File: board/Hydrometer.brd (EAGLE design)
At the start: 49.2 x 49.5 mm, 13 parts, among them IC2 REG1117

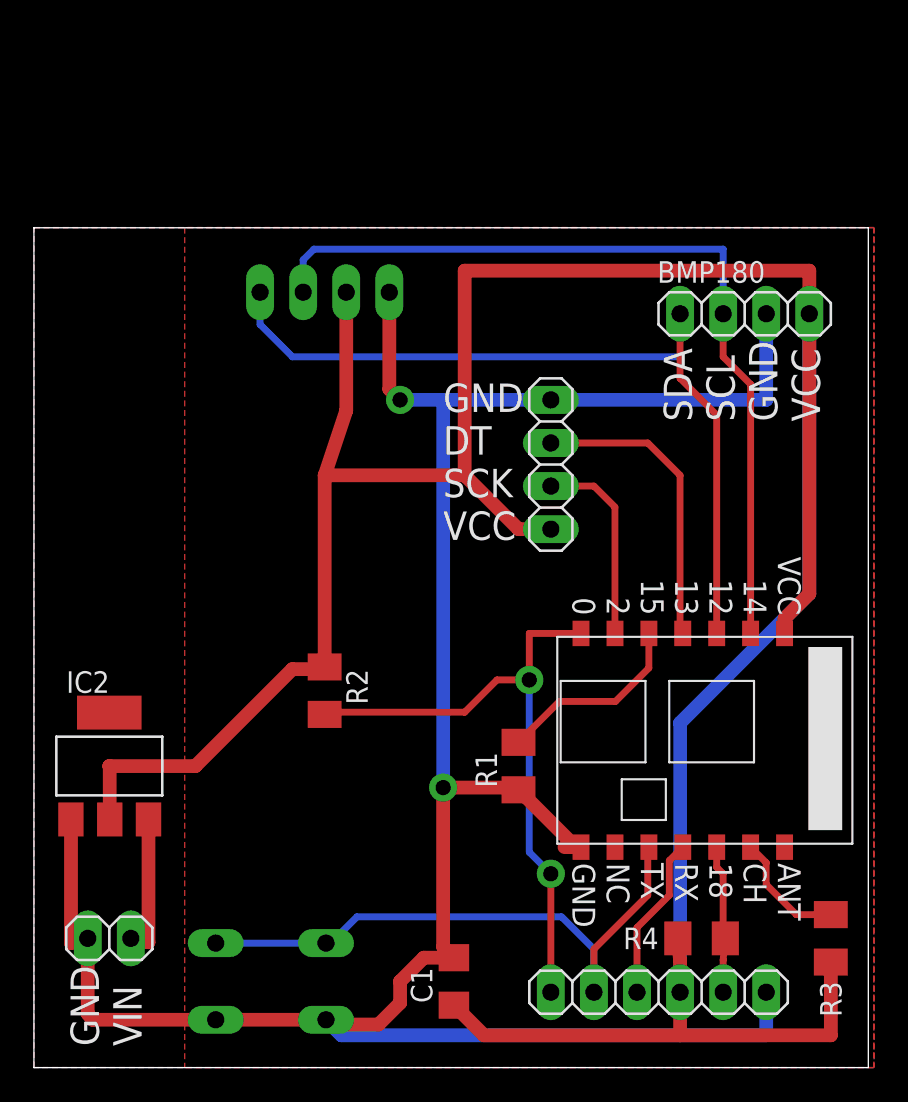
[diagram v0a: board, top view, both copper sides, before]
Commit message: Update board layout to a (mostly) single sided PCB
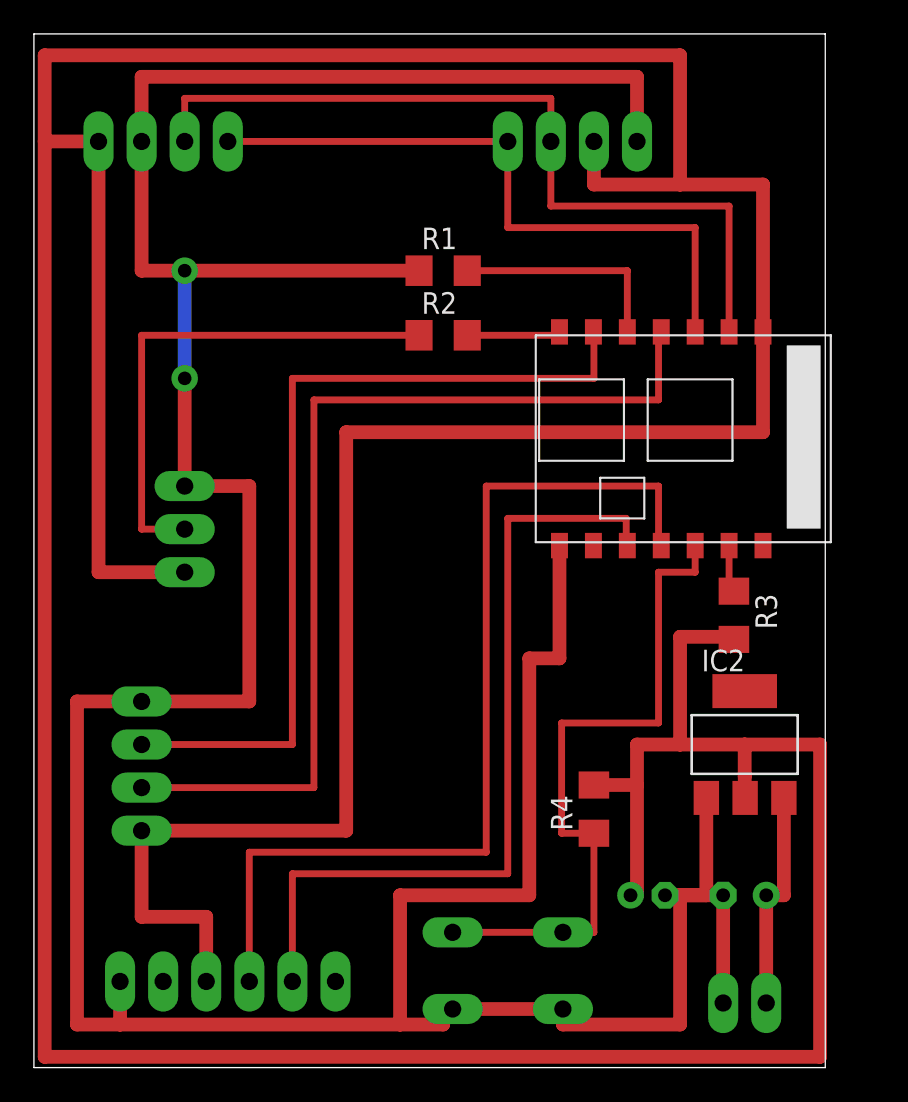
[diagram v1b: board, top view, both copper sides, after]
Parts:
- added C2: 47uF, resistor:E2,5-5
- added JP2: (no value), pinhead:1X03
- C1: value 100nF -> 47uF; device resistor:C1206 -> resistor:E2-5
- R1, R2, R3, R4: device resistor:M1206 -> resistor:R1206
- S1: value RST -> ACT
- moved PWR 37.7 mm to (41.9, 3.81), flipped to the bottom, turned to 0 degrees
- moved IC2 37.5 mm to (41.9, 19.1)
- moved BMP180 35.8 mm to (7.62, 54.6), flipped to the bottom
- moved HX711 30.0 mm to (6.35, 17.8), flipped to the bottom
- moved R1 29.5 mm to (24.1, 47.0), turned to 0 degrees
- moved JP1 25.4 mm to (11.4, 5.08), flipped to the bottom
- moved R2 22.1 mm to (24.1, 43.2), turned to 0 degrees
- moved R3 19.9 mm to (41.3, 26.7)
- moved U$1 17.8 mm to (47.0, 43.2)
- moved OLED 17.1 mm to (31.8, 54.6)
- moved S1 14.0 mm to (27.9, 5.71)
- moved C1 12.5 mm to (36.2, 10.2), flipped to the bottom, turned to 180 degrees
- moved R4 9.92 mm to (33.0, 15.2), turned to 90 degrees
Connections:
- removed net RTS: JP1.2, R4.1, U$1.GPIO18
- new net BTN: R4.1, S1.3, S1.4, U$1.GPIO18
- new net N$2: JP2.2, R2.1
- net +5V: now also C2.+
- net DT: now also U$1.GPIO2; no longer U$1.GPIO13
- net DTR: no longer JP1.6
- net GND: now also C1.-, C2.-, JP2.3; no longer C1.2
- net SCK: now also U$1.GPIO13; no longer U$1.GPIO2
- net TX: no longer S1.3, S1.4
- net VCC: now also C1.+, JP2.1; no longer C1.1, R2.1
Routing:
- net VCC: track 185.8 -> 337.3 mm
- net GND: track 142.9 -> 223.3 mm
- net RX: track 9.67 -> 57.0 mm
- net SCK: track 11.7 -> 57.5 mm
- net BTN: track 0.00 -> 40.9 mm
- net DT: track 17.8 -> 51.0 mm
- net DTR: track 37.6 -> 5.64 mm, vias 2 -> 0
- net N$2: track 0.00 -> 30.3 mm
- net TX: track 36.2 -> 48.7 mm
- net RTS: track 9.03 -> 0.00 mm
- net SDA: track 47.2 -> 38.8 mm
- net +5V: track 8.31 -> 13.1 mm
- net N$5: track 7.13 -> 2.97 mm
- net SCL: track 50.3 -> 48.4 mm
- net N$3: track 11.5 -> 13.0 mm
- removed copper zone on layer 1, net GND
- removed copper zone on layer 16, net GND
- removed copper zone on layer 1, net N$1
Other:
- board size 49.2 x 49.5 mm -> 46.7 x 61 mm
- board text added: "GND VCC SCL SDA"
- board text added: "PGM RUN"
- board text added: "TX RX VCC GND"
- board text removed: "ANT CH 18 RX TX NC GND"
- board text removed: "GND VIN"
- board text removed: "VCC 14 12 13 15 2 0"
- board text removed: "VCC GND SCL SDA"

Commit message: Add fill planes to board
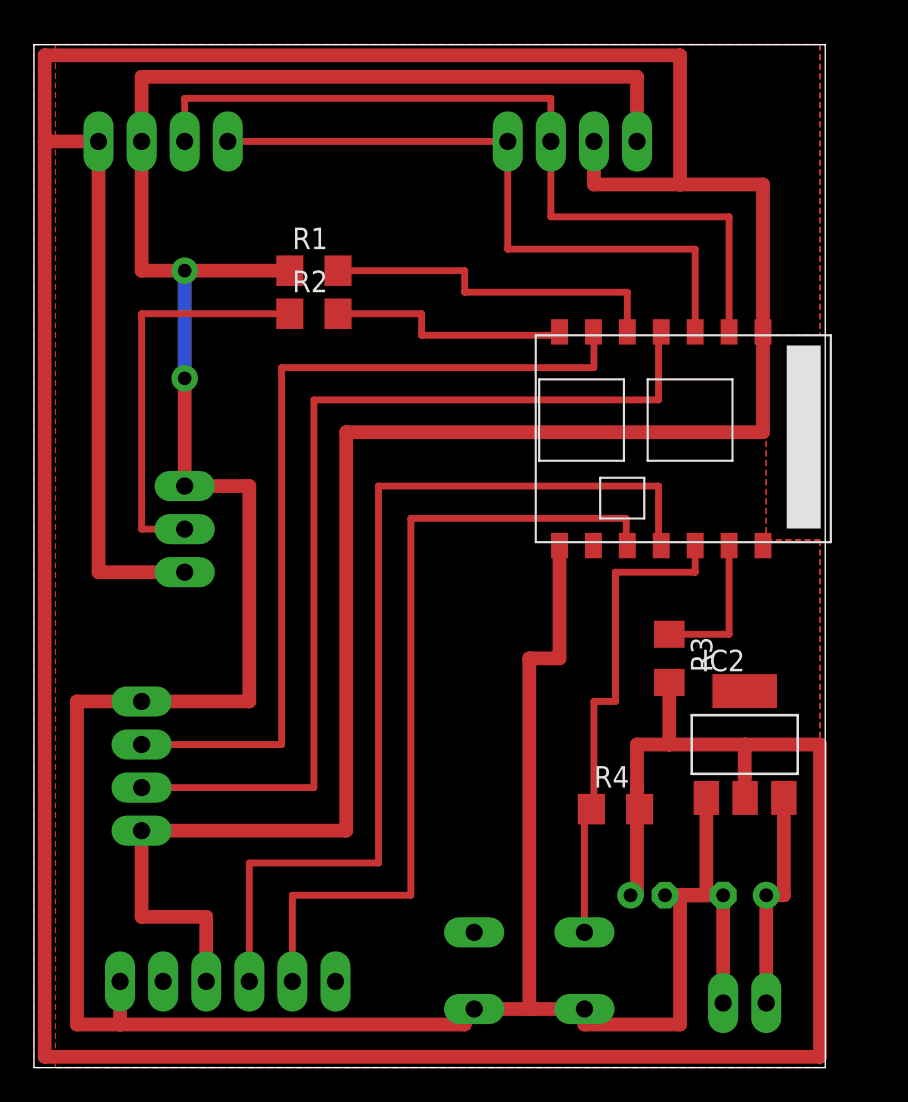
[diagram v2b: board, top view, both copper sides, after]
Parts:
- JP2: value (none) -> MODE
- moved R2 7.73 mm to (16.5, 44.5)
- moved R1 7.62 mm to (16.5, 47.0)
- moved R3 4.58 mm to (37.5, 24.1)
- moved S1 1.27 mm to (29.2, 5.71)
- moved R4 1.27 mm to (34.3, 15.2), turned to 0 degrees
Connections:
- net BTN: no longer S1.3
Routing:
- net GND: track 223.3 -> 207.1 mm
- net BTN: track 40.9 -> 29.3 mm
- net DTR: track 5.64 -> 14.5 mm
- net VCC: track 337.3 -> 328.9 mm
- net N$3: track 13.0 -> 20.7 mm
- net N$2: track 30.3 -> 24.0 mm
- net N$5: track 2.97 -> 8.75 mm
- added copper zone on layer 1, net GND
- added copper zone on layer 1, net N$1
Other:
- board size 46.7 x 61 mm -> 46.7 x 60.3 mm

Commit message: Add input protection and power LED
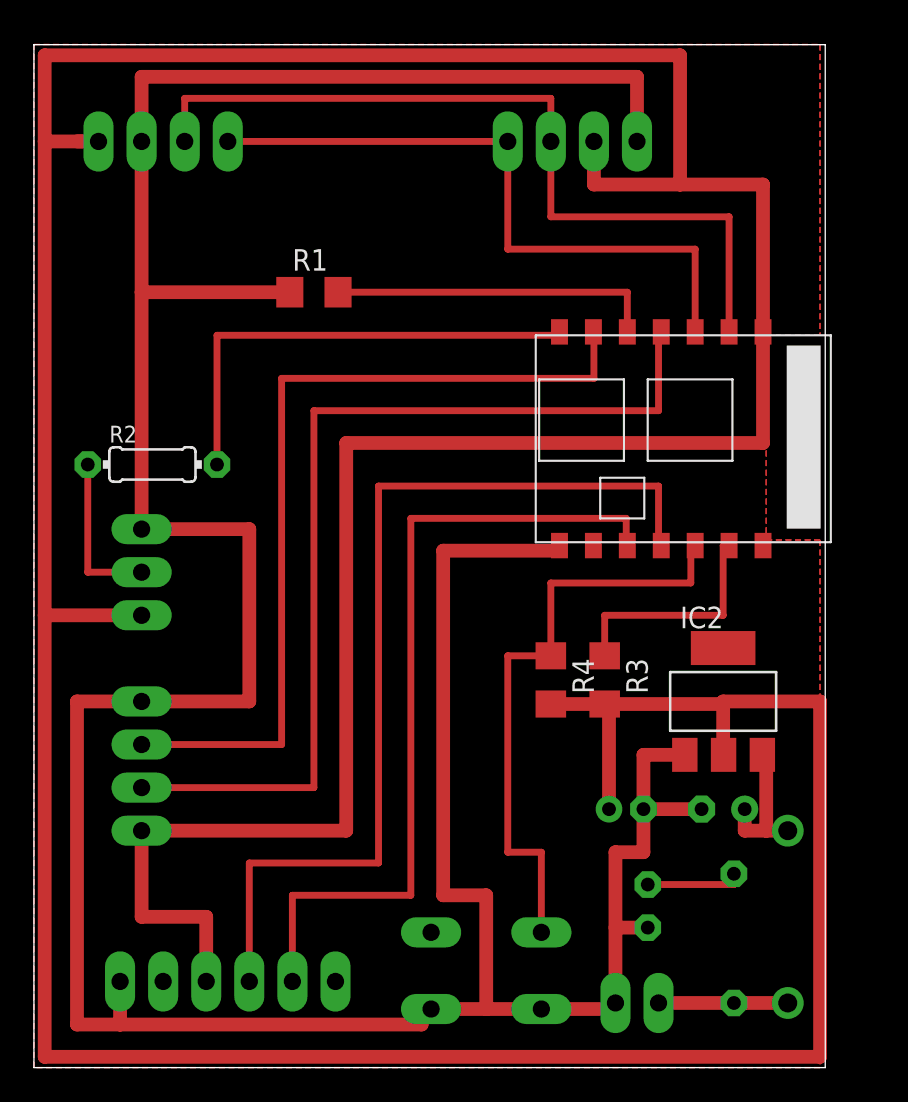
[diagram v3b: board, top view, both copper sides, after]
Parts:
- added D1: 1N4001, diode:DO41-10
- added LED1: (no value), led:LED3MM
- added R5: 150R, resistor:0204/7
- R2: device resistor:R1206 -> resistor:0204/7
- moved R2 13.0 mm to (6.99, 35.6)
- moved R4 8.52 mm to (30.5, 22.9), turned to 270 degrees
- moved PWR 6.35 mm to (35.6, 3.81)
- moved C1 5.24 mm to (34.9, 15.2)
- moved C2 5.24 mm to (40.6, 15.2)
- moved R3 4.02 mm to (33.7, 22.9)
- moved JP2 3.59 mm to (6.35, 29.2)
- moved IC2 2.84 mm to (40.6, 21.6)
- moved S1 2.54 mm to (26.7, 5.71)
- moved R1 1.27 mm to (16.5, 45.7)
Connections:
- new net N$4: D1.A, PWR.1, R5.2
- new net N$8: LED1.A, R5.1
- net +5V: now also D1.C; no longer PWR.1
- net GND: now also LED1.K
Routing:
- net VCC: track 328.9 -> 306.4 mm
- net N$2: track 24.0 -> 9.53 mm
- net DTR: track 14.5 -> 28.0 mm
- net N$4: track 0.00 -> 7.62 mm
- net BTN: track 29.3 -> 35.8 mm
- net N$8: track 0.00 -> 5.71 mm
- net N$5: track 8.75 -> 13.8 mm
- net +5V: track 13.1 -> 8.51 mm
- net GND: track 207.1 -> 210.8 mm, vias 2 -> 0
- net N$3: track 20.7 -> 19.4 mm
